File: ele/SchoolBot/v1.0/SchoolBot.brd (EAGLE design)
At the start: 100.1 x 58.3 mm, 55 parts, among them X1 M8, X2 M8, X4 POWER_IN

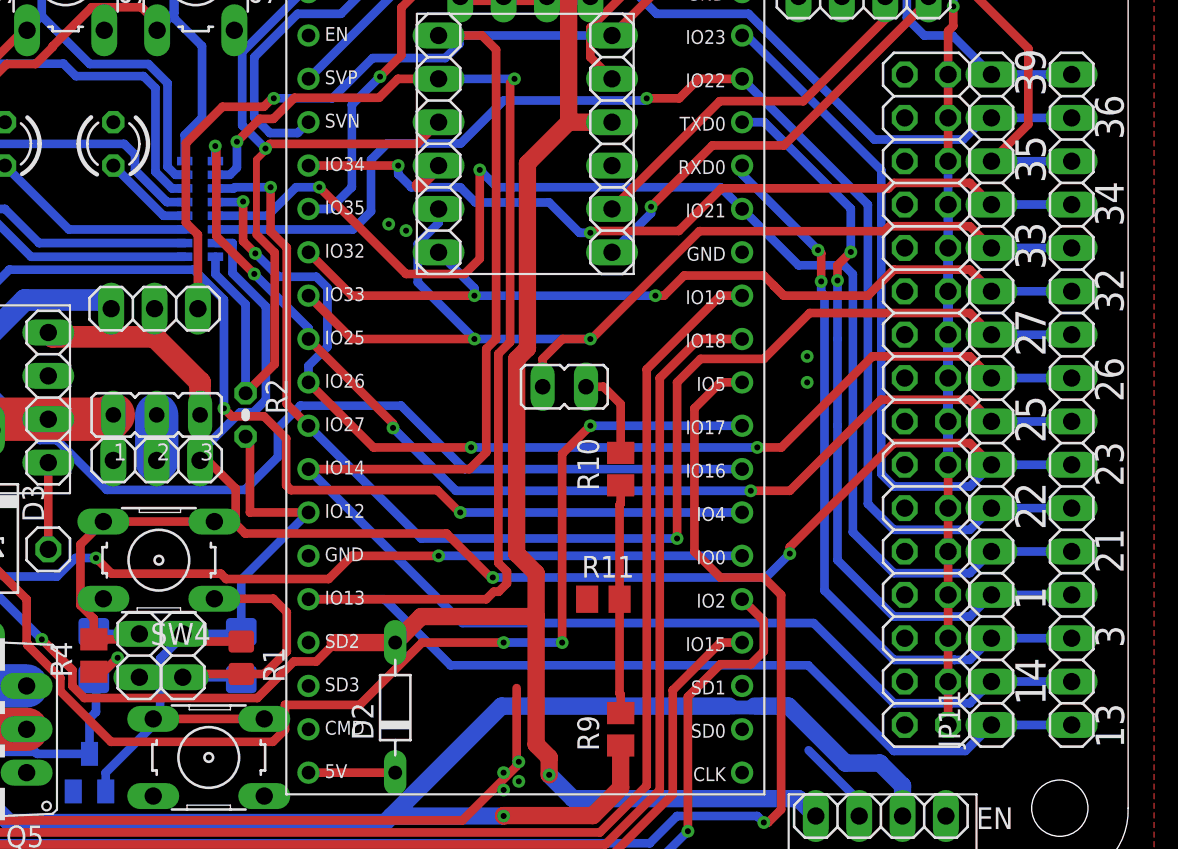
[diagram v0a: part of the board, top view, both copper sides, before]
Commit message: off pin
presun vypinani desky na pin 13 kvuli nahrav8ni programu
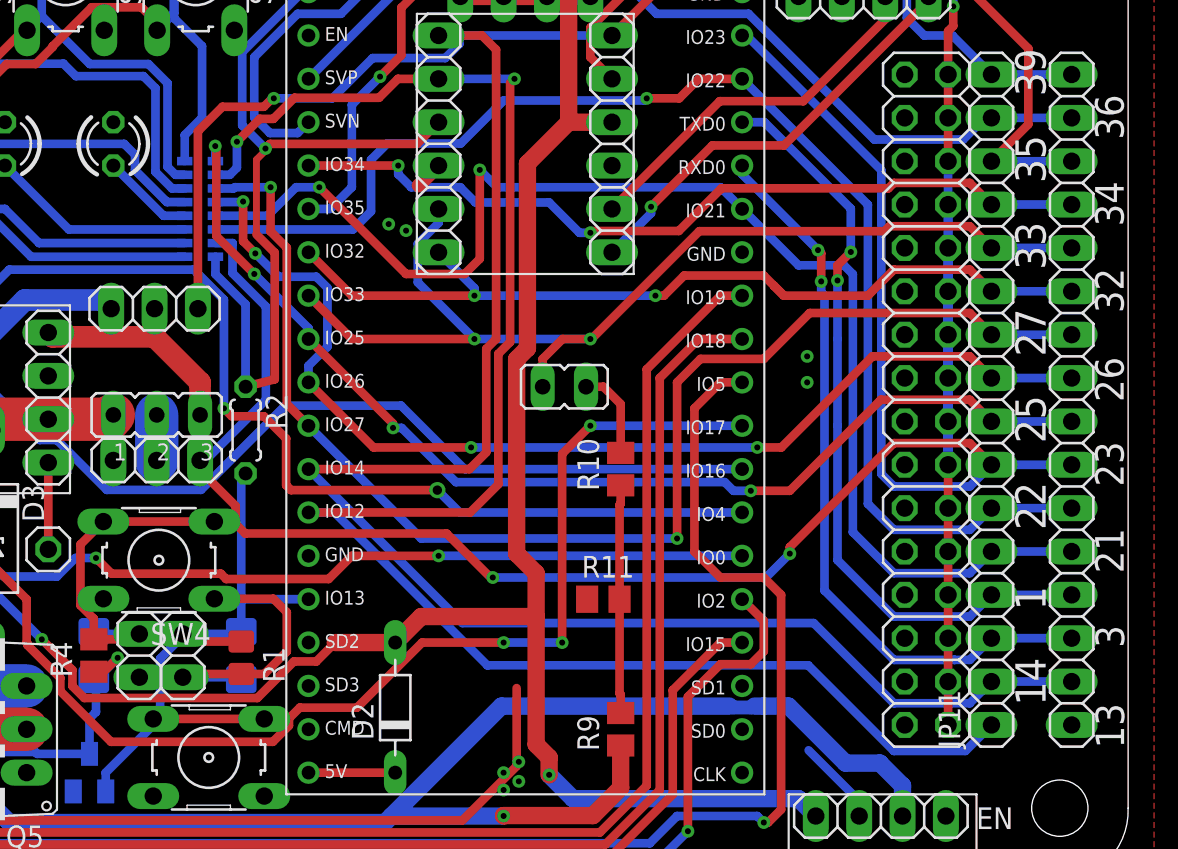
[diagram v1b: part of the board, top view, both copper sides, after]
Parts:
- R2: device rcl_upravena:0204V -> rcl_upravena:0204/5
- moved R2 0.89 mm to (43.3, 25.1)
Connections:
- removed net GPIO13: IM11.2, IM6.15, JP11.1, JP8.1, RN1.2
- new net GPIO12: IM11.2, IM6.13, JP11.1, JP8.1, RN1.2
- net OFF: now also IM6.15; no longer IM6.13
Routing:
- net GPIO13: track 111.9 -> 0.00 mm, vias 2 -> 0
- net GPIO12: track 0.00 -> 103.1 mm, vias 0 -> 2
- net OFF: track 41.4 -> 38.1 mm
- net PWM3: track 57.1 -> 56.1 mm
- net PWM1: track 71.3 -> 70.7 mm
- net GPIO14-5V: track 50.9 -> 50.4 mm
- net GPIO23: track 112.2 -> 111.7 mm
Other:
- board text added: "C1"
- board text added: "C2"

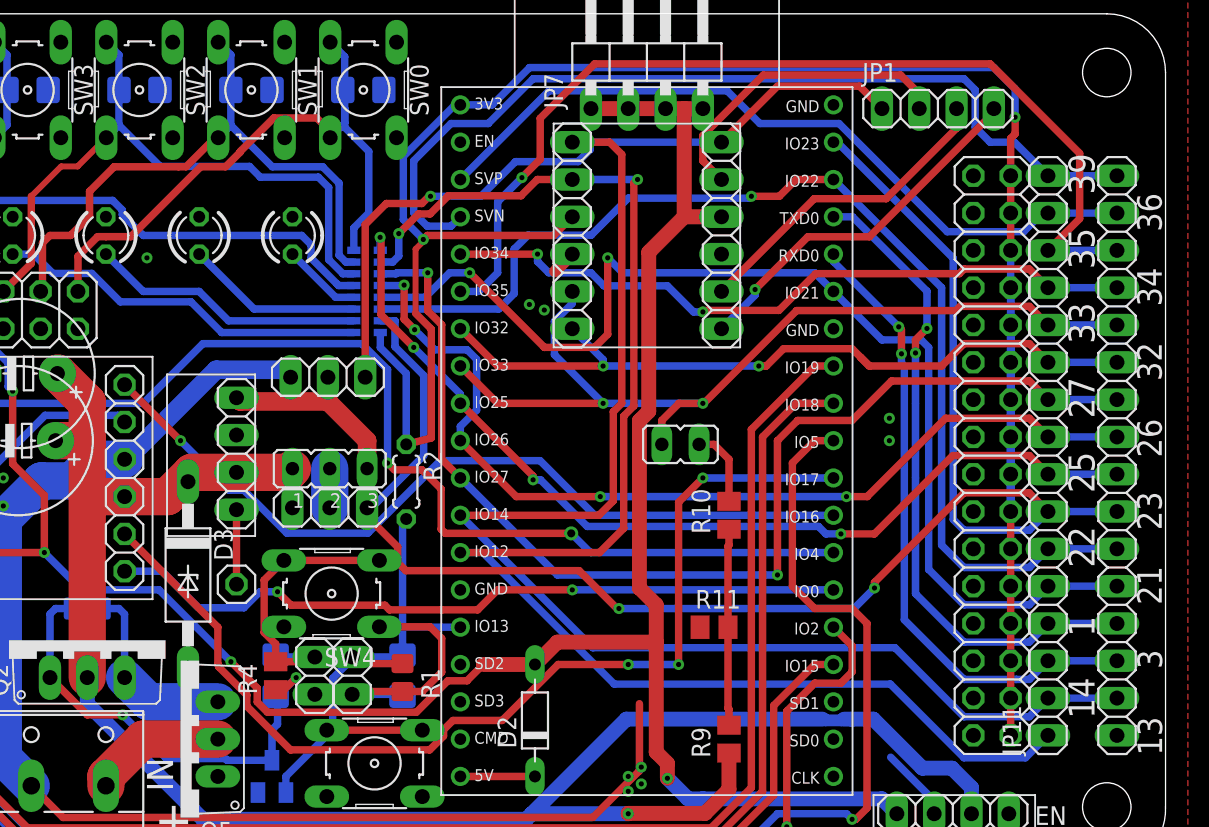
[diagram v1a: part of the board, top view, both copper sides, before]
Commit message: program ovladani serv
zatim jen s lehce upravenym RBControl
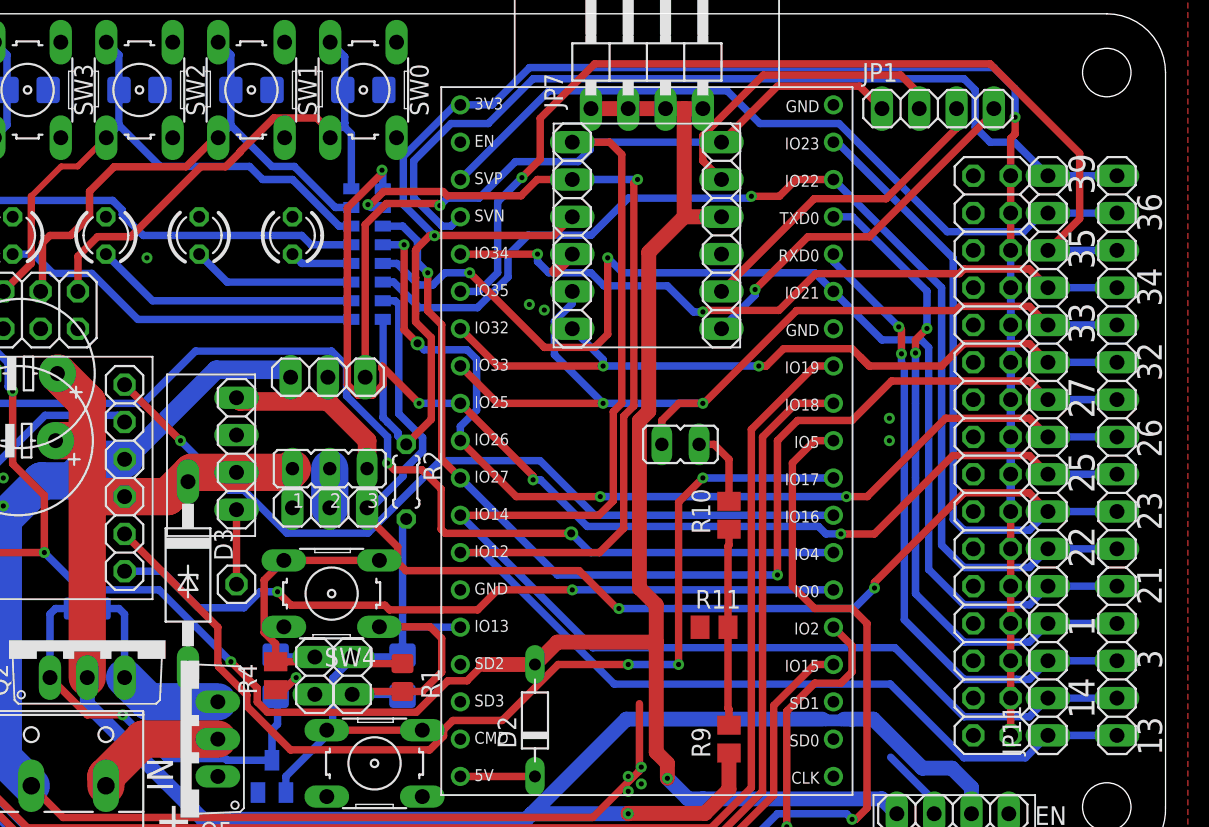
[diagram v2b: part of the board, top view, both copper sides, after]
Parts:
- removed RN1: (no value), resistor-array:742-16NS
- added RN2, RN3: (no value), resistor-dil:EXBS8V
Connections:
- net +3V3: now also RN3.4; no longer RN1.8
- net GPIO12: now also RN2.2; no longer RN1.2
- net GPIO21: now also RN3.1; no longer RN1.5
- net GPIO22: now also RN3.2; no longer RN1.6
- net GPIO23: now also RN3.3; no longer RN1.7
- net GPIO25: now also RN2.1; no longer RN1.1
- net GPIO26: now also RN2.4; no longer RN1.4
- net GPIO27: now also RN2.3; no longer RN1.3
- net LED0: now also RN3.8; no longer RN1.12
- net LED1: now also RN3.7; no longer RN1.11
- net LED2: now also RN3.6; no longer RN1.10
- net LED3: now also RN3.5; no longer RN1.9
- net SW0: now also RN2.8; no longer RN1.16
- net SW1: now also RN2.7; no longer RN1.15
- net SW2: now also RN2.6; no longer RN1.14
- net SW3: now also RN2.5; no longer RN1.13
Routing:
- net GPIO25: track 65.7 -> 78.8 mm
- net +3V3: track 183.5 -> 189.8 mm
- net SW0: track 42.5 -> 36.4 mm
- net SW1: track 41.6 -> 37.0 mm
- net SW2: track 44.3 -> 39.9 mm
- net GPIO12: track 103.1 -> 107.5 mm
- net GPIO26: track 65.0 -> 68.0 mm
- net GPIO27: track 76.9 -> 78.9 mm
- net ENC_A1: track 81.2 -> 79.2 mm
- net SW3: track 46.6 -> 44.8 mm
- net GPIO23: track 111.7 -> 112.8 mm
- net LED0: track 5.40 -> 4.27 mm
- net LED1: track 12.1 -> 11.1 mm
- net LED2: track 18.8 -> 18.0 mm
- net GPIO39: track 61.8 -> 61.2 mm
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
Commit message: new board
-komplenti prekreslini desky
-doplneni rady pinhedu gnd pro 5v piniste
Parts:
- JP1: device pinhead:1X04 -> pinhead:2X04
- JP7: device pinhead:1X04/90 -> pinhead:1X04
- moved JP1 177.4 mm to (-88.9, -5.08)
- moved JP7 163.0 mm to (-88.9, -12.7)
- moved IM3 152.8 mm to (-67.3, 58.4), turned to 0 degrees
- moved JP8 148.4 mm to (-34.3, 105.4), turned to 0 degrees
- moved JP11 148.0 mm to (-34.3, 111.8), turned to 0 degrees
- moved R9 145.6 mm to (-47.0, 100.3), turned to 0 degrees
- moved D2 145.6 mm to (-38.1, 123.2), turned to 0 degrees
- moved R2 143.3 mm to (-78.7, 100.3), turned to 0 degrees
- moved LED1 142.7 mm to (-91.4, 118.1), turned to 0 degrees
- moved C5 140.5 mm to (-94.0, 92.7), flipped to the top
- moved SW5 139.9 mm to (-81.3, 73.7), turned to 0 degrees
- moved JP2 138.4 mm to (-55.9, 100.3), turned to 0 degrees
- moved Q5 137.4 mm to (-83.8, 87.6), turned to 0 degrees
- moved Q6 133.7 mm to (-61.0, 99.1), flipped to the top
- moved R11 132.1 mm to (-36.8, 100.3)
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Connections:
- net GND: now also JP1.2, JP1.4, JP1.6, JP1.8
- net GPIO13-5V: now also JP1.3; no longer JP1.2
- net GPIO32_5V: now also JP1.7; no longer JP1.4
- net GPIO33_5V: now also JP1.5; no longer JP1.3
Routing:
- net +3V3: track 189.8 -> 0.00 mm, vias 2 -> 0
- net +5V: track 162.6 -> 0.00 mm, vias 4 -> 0
- net VCC: track 133.4 -> 0.00 mm, vias 1 -> 0
- net PWM2: track 126.1 -> 0.00 mm, vias 1 -> 0
- net GND: track 117.8 -> 0.00 mm, vias 14 -> 0
- net ENC_B1: track 113.4 -> 0.00 mm
- net GPIO23: track 112.8 -> 0.00 mm, vias 2 -> 0
- net ENC_B2: track 107.9 -> 0.00 mm
- net GPIO12: track 107.5 -> 0.00 mm, vias 2 -> 0
- net ENC_A2: track 105.7 -> 0.00 mm
- net SLEEP: track 104.5 -> 0.00 mm, vias 1 -> 0
- net GPIO14: track 89.3 -> 0.00 mm
- net ENC_A1: track 79.2 -> 0.00 mm, vias 2 -> 0
- net GPIO27: track 78.9 -> 0.00 mm, vias 2 -> 0
- net GPIO25: track 78.8 -> 0.00 mm, vias 4 -> 0
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- removed copper zone on layer 1, net GND
- removed copper zone on layer 16, net GND
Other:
- board size 100.1 x 58.3 mm -> 90 x 66 mm
- board text removed: "+"
- board text removed: "-"
- board text removed: "1"
- board text removed: "13"
- board text removed: "14"
- board text removed: "21"
- board text removed: "22"
- board text removed: "23"
- board text removed: "25"
- board text removed: "26"
- board text removed: "27"
- board text removed: "3"
- board text removed: "3.3V"
- board text removed: "32"
- board text removed: "33"
- board text removed: "34"
- board text removed: "35"
- board text removed: "36"
- board text removed: "39"
- board text removed: "3V"
- board text removed: "5V"
- board text removed: "BLUE"
- board text removed: "Battery"
- board text removed: "C1"
- board text removed: "C2"
- board text removed: "EN"
- board text removed: "ENC_A1"
- board text removed: "ENC_A2"
- board text removed: "ENC_B1"
- board text removed: "ENC_B2"
- board text removed: "GND"
- board text removed: "GPIO13"
- board text removed: "GPIO15"
- board text removed: "GREEN"
- board text removed: "IN"
- board text removed: "IO13"
- board text removed: "IO14"
- board text removed: "IO15"
- board text removed: "IO32"
- board text removed: "IO33"
- board text removed: "M1"
- board text removed: "M2"
- board text removed: "MA1"
- board text removed: "MA2"
- board text removed: "MB1"
- board text removed: "MB2"
- board text removed: "OFF"
- board text removed: "ON"
- board text removed: "OUT1"
- board text removed: "OUT2"
- board text removed: "OUT3"
- board text removed: "OUT4"
- board text removed: "P-LED"
- board text removed: "PWM0"
- board text removed: "PWM1"
- board text removed: "PWM2"
- board text removed: "PWM3"
- board text removed: "RB3202-SchoolBot v0.1"
- board text removed: "RED"
- board text removed: "RX"
- board text removed: "S-leds"
- board text removed: "S-servo"
- board text removed: "SLEEP"
- board text removed: "SW0"
- board text removed: "SW1"
- board text removed: "SW2"
- board text removed: "SW3"
- board text removed: "ServoS-5V"
- board text removed: "TX"
- board text removed: "ULT"
- board text removed: "V5"
- board text removed: "VCC"

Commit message: nove rozlozeni
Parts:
- removed J2: (no value), jumper:JP2
- removed JP13, JP15: (no value), pinhead:1X06
- removed JP14: (no value), pinhead:1X03
- added JP16: (no value), pinhead:2X04
- added JP42, JP47, JP48: 292161-3, iServo_connector:292161-3
- added JP9: (no value), pinhead:2X05
- added R8: 10k, rcl_upravena:R0805
- JP3: value START_BUTTON -> (none); device pinhead:1X02 -> pinhead:1X04
- JP4: device pinhead:2X04 -> pinhead:2X03
- JP6: value STOP_BUTTON -> (none); device pinhead:1X02 -> pinhead:2X04
- R2: device rcl_upravena:0204/5 -> rcl_upravena:R0805
- moved JP7 169.1 mm to (79.5, 2.79)
- moved JP1 168.8 mm to (79.5, 6.60), turned to 180 degrees
- moved IM4 151.7 mm to (68.1, 11.4), turned to 90 degrees
- moved IM3 147.2 mm to (74.2, 17.8), turned to 270 degrees
- moved JP12 144.2 mm to (71.1, 14.5), turned to 90 degrees
- moved SW5 142.3 mm to (43.9, 6.10), turned to 270 degrees
- moved SW4 140.7 mm to (52.3, 6.10), turned to 270 degrees
- moved JP10 140.6 mm to (55.9, 12.7)
- moved R3 140.5 mm to (41.9, 14.7), turned to 90 degrees
- moved R2 138.7 mm to (37.8, 25.1), turned to 270 degrees
- moved LED1 138.7 mm to (27.9, 47.5), turned to 180 degrees
- moved JP2 136.9 mm to (66.0, 38.1), turned to 270 degrees
- moved C5 134.9 mm to (35.3, 54.4), flipped to the bottom
- moved Q5 133.7 mm to (28.4, 15.0)
- moved JP3 133.3 mm to (79.5, 10.4), turned to 180 degrees
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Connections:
- net BAT_PROT1 renamed BAT_POL+
- removed net N$3: J2.2, JP14.2
- removed net START_BUTTON1: C1.2, JP3.1, R4.2, SW4.3, SW4.4
- new net EN: JP16.4, R8.1
- new net N$5: JP9.10, JP9.2, JP9.4, JP9.6, JP9.8
- new net N$7: C1.2, JP16.6, R4.2, SW4.3, SW4.4
- net +3V3: now also R8.2
- net +5V: now also JP1.2, JP1.4, JP1.6, JP1.8, JP16.2, JP6.1, JP6.2; no longer JP13.2, JP15.2, JP7.1, JP7.2, JP7.3, JP7.4
- net ENC_A1: now also JP6.6; no longer JP13.3
- net ENC_A2: now also JP6.3; no longer JP15.4
- net ENC_B1: now also JP6.4; no longer JP13.4
- net ENC_B2: now also JP6.5; no longer JP15.3
- net GND: now also JP16.1, JP16.3, JP16.5, JP16.7, JP42.1, JP47.1, JP48.1, JP6.7, JP6.8, JP7.1, JP7.2, JP7.3, JP7.4; no longer JP1.2, JP1.4, JP1.6, JP1.8, JP13.5, JP14.1, JP15.5, JP3.2, JP4.7, JP6.2
- net GPIO13-5V: now also JP3.2
- net GPIO14-5V: now also JP3.1
- net GPIO23: now also JP42.3, JP47.3, JP48.3; no longer JP14.3
- net GPIO32_5V: now also JP3.4
- net GPIO33_5V: now also JP3.3
- net LED0: now also JP9.1
- net LED1: now also JP9.3
- net LED2: now also JP9.5
- net LED3: now also JP9.7
- net M1A: now also X1.1; no longer JP13.1, X1.2
- net M1B: now also X1.2; no longer JP13.6, X1.1
- net M2A: no longer JP15.1
- net M2B: no longer JP15.6
- net OFF: now also JP16.8; no longer JP6.1
- net SERVO_STEPDOWN_5V: no longer J2.3
- net SW0: now also JP4.6; no longer JP4.8
- net SW1: now also JP4.4; no longer JP4.6
- net SW2: now also JP4.2; no longer JP4.4
- net SW3: now also JP9.9; no longer JP4.2
- net VCC: now also JP42.2, JP47.2, JP48.2; no longer J2.1
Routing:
- net +3V3: track 0.00 -> 43.2 mm
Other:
- board size 90 x 66 mm -> 95 x 60 mm

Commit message: new_board
nesting noveho rozlozeni
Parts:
- removed JP12: (no value), pinhead:1X03
- moved JP6 48.8 mm to (4.57, 34.5), turned to 270 degrees
- moved JP10 33.4 mm to (89.0, 16.6)
- moved D3 30.1 mm to (54.6, 14.0)
- moved LED0 22.9 mm to (12.7, 47.5)
- moved LED3 22.9 mm to (35.6, 47.5)
- moved C1 20.8 mm to (33.0, 33.5), turned to 180 degrees
- moved R3 20.8 mm to (33.0, 33.5), turned to 180 degrees
- moved Q6 16.9 mm to (33.3, 30.5), turned to 90 degrees
- moved R4 16.8 mm to (33.0, 30.5), turned to 180 degrees
- moved RN2 14.5 mm to (36.8, 42.2)
- moved Q5 13.4 mm to (41.1, 10.8), turned to 180 degrees
- moved C2 13.0 mm to (33.0, 27.4), turned to 0 degrees
- moved R1 13.0 mm to (33.0, 27.4), turned to 180 degrees
- moved R8 10.9 mm to (40.6, 33.0), flipped to the top, turned to 0 degrees
- moved IM3 10.5 mm to (63.6, 18.0)
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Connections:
- net N$7 renamed ON
- removed net N$5: JP9.10, JP9.2, JP9.4, JP9.6, JP9.8
- removed net N$6: IM6.2
- net +5V: no longer JP1.2, JP1.4, JP1.6, JP1.8
- net EN: now also IM6.2
- net ENC_B1: now also IM6.31; no longer IM6.23
- net ENC_B2: now also IM6.23; no longer IM6.31
- net GND: now also JP9.10, JP9.2, JP9.4, JP9.6, JP9.8; no longer JP12.1
- net GPIO12: now also IM11.6, JP11.6, JP8.6; no longer IM11.2, JP11.1, JP8.1
- net GPIO14: now also IM11.5, JP11.7, JP8.7; no longer IM11.1, JP11.2, JP8.2
- net GPIO14-5V: no longer JP12.3
- net GPIO22: now also JP11.2, JP8.2; no longer JP11.6, JP8.6
- net GPIO23: now also JP11.1, JP8.1; no longer JP11.7, JP8.7
- net GPIO25: now also JP11.10, JP8.10; no longer JP11.8, JP8.8
- net GPIO27: now also JP11.8, JP8.8; no longer JP11.10, JP8.10
- net GPIO32: now also IM11.1, JP11.12, JP8.12; no longer IM11.6, JP11.11, JP8.11
- net GPIO33: now also IM11.2, JP11.11, JP8.11; no longer IM11.5, JP11.12, JP8.12
- net GPIO34: now also JP11.14, JP8.14; no longer JP11.13, JP8.13
- net GPIO35: now also JP11.13, JP8.13; no longer JP11.14, JP8.14
- net GPIO36: now also JP11.16, JP8.16; no longer JP11.15, JP8.15
- net GPIO39: now also JP11.15, JP8.15; no longer JP11.16, JP8.16
- net SERVO_STEPDOWN_5V: now also JP1.2, JP1.4, JP1.6, JP1.8; no longer JP12.2
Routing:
- net GPIO12: track 0.00 -> 52.6 mm
- net GPIO25: track 0.00 -> 44.3 mm, vias 0 -> 1
- net GPIO26: track 0.00 -> 41.7 mm
- net GPIO27: track 0.00 -> 38.6 mm
- net SW2: track 0.00 -> 36.8 mm, vias 0 -> 1
- net SW3: track 0.00 -> 36.7 mm
- net SW0: track 0.00 -> 35.6 mm, vias 0 -> 1
- net SW1: track 0.00 -> 35.5 mm, vias 0 -> 1
- net GPIO14: track 0.00 -> 32.8 mm
- net GPIO21: track 0.00 -> 31.7 mm, vias 0 -> 1
- net GPIO32: track 0.00 -> 30.3 mm
- net GPIO33: track 0.00 -> 30.3 mm
- net LED1: track 0.00 -> 29.6 mm
- net LED0: track 0.00 -> 28.8 mm
- net GPIO22: track 0.00 -> 23.7 mm
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- added copper zone on layer 1, net BAT1
- added copper zone on layer 16, net VCC

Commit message: nove rozlozeni
konecne zaroutovano
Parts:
- removed R10: 1k, resistor:M0805
- removed R11: 3k9, resistor:M0805
- removed R9: 10k, resistor:M0805
- added R5: (no value), pot:SM-42/43X
- moved C1 8.52 mm to (25.0, 30.6)
- moved R3 8.52 mm to (25.0, 30.6)
- moved R2 8.47 mm to (33.3, 26.3)
- moved R8 8.41 mm to (33.0, 36.6)
- moved R4 8.16 mm to (25.4, 27.6)
- moved Q6 8.16 mm to (25.7, 27.6)
- moved C2 8.03 mm to (25.4, 24.9)
- moved R1 8.03 mm to (25.4, 24.9)
- moved JP2 1.62 mm to (66.0, 40.5)
- moved D2 0.28 mm to (45.1, 42.4)
- moved JP10 0.18 mm to (88.9, 16.8)
- moved JP48 0.13 mm to (62.1, 5.59)
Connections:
- removed net N$2: JP2.1, R10.2
- removed net N$4: R10.1, R11.2, R9.2
- new net BAT-REF: JP2.1, R5.2
- net GND: now also R5.3; no longer R11.1
- net GPIO23: no longer JP42.3, JP47.3, JP48.3
- net GPIO33: no longer JP2.2
- net GPIO34: now also JP2.2
- net GPIO35: now also JP42.3, JP47.3, JP48.3
- net PWM0: now also IM6.29; no longer IM6.25
- net PWM2: now also IM6.27; no longer IM6.29
- net PWM3: now also IM6.25; no longer IM6.27
- net VCC: now also R5.1; no longer R9.1
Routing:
- net OFF: track 0.00 -> 95.6 mm, vias 0 -> 4
- net +5V: track 0.00 -> 93.3 mm, vias 0 -> 2
- net IO3: track 3.30 -> 81.4 mm
- net IO1: track 3.30 -> 78.4 mm
- net ON: track 0.00 -> 74.3 mm, vias 0 -> 2
- net GPIO21: track 31.7 -> 104.9 mm
- net EN: track 0.00 -> 72.7 mm, vias 0 -> 2
- net SLEEP: track 0.00 -> 71.1 mm, vias 0 -> 1
- net ENC_A2: track 0.00 -> 70.4 mm, vias 0 -> 1
- net ENC_B1: track 0.00 -> 69.8 mm, vias 0 -> 1
- net GPIO35: track 13.2 -> 80.7 mm, vias 0 -> 1
- net PWM2: track 0.00 -> 64.3 mm, vias 0 -> 1
- net GPIO23: track 20.4 -> 83.5 mm, vias 0 -> 3
- net PWM3: track 0.00 -> 60.1 mm, vias 0 -> 1
- net PWM0: track 0.00 -> 59.2 mm, vias 0 -> 1
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- added copper zone on layer 1, net +5V
- added copper zone on layer 1, net GND
- added copper zone on layer 16, net GND
- added copper zone on layer 1, net M1A
- added copper zone on layer 16, net M1B
- added copper zone on layer 1, net M2A
- added copper zone on layer 16, net M2B
